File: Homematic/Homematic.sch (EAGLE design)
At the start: 28 parts, among them IC1 3.3V, IC2 3.3V, P1 DF11-06-2DS, Q1 BS170

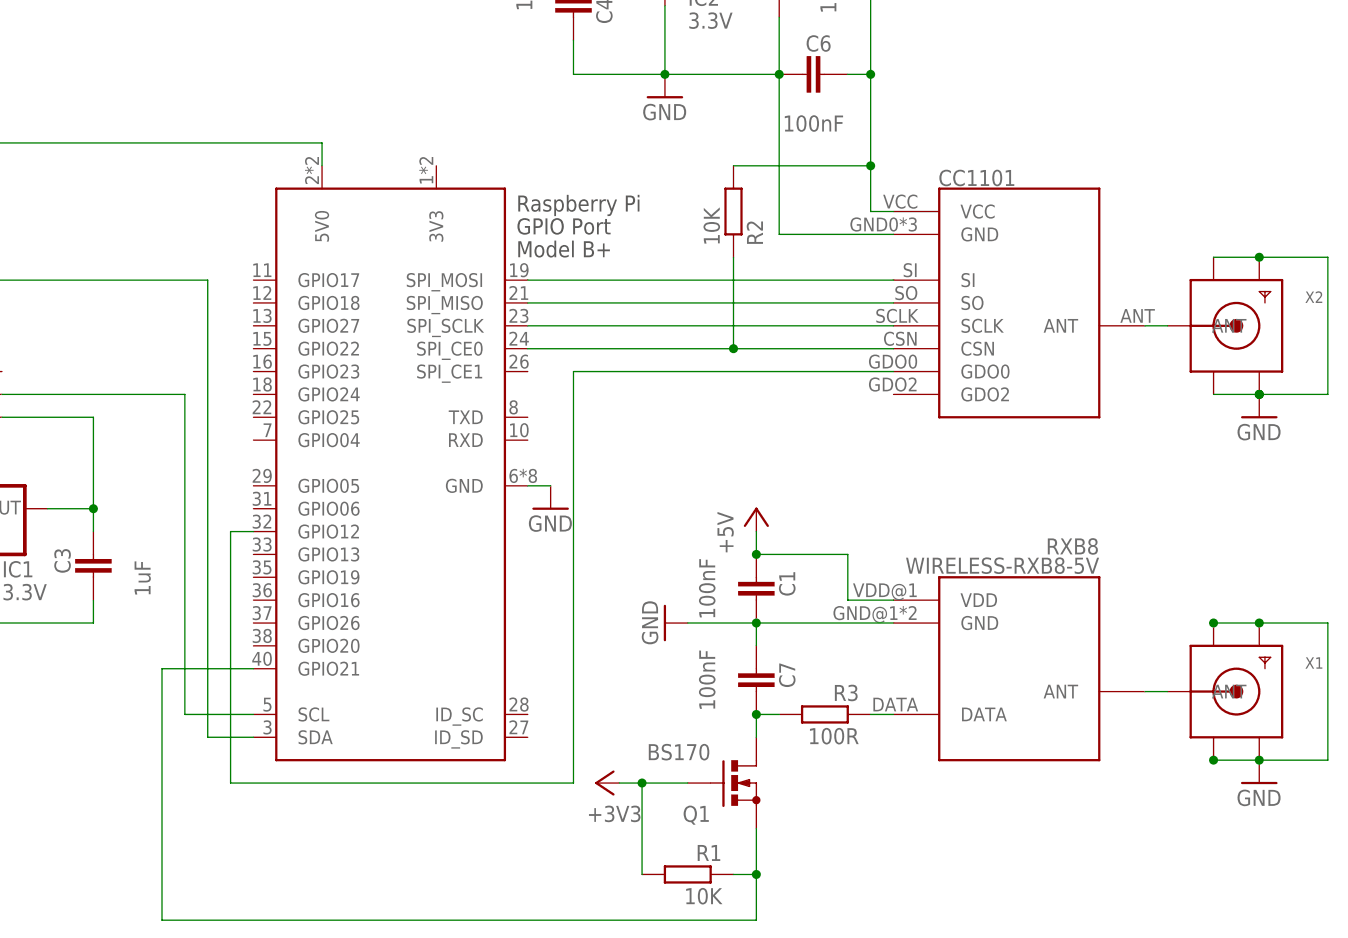
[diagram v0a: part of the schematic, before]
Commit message: Replace RXB8 with CC1101 receiver.
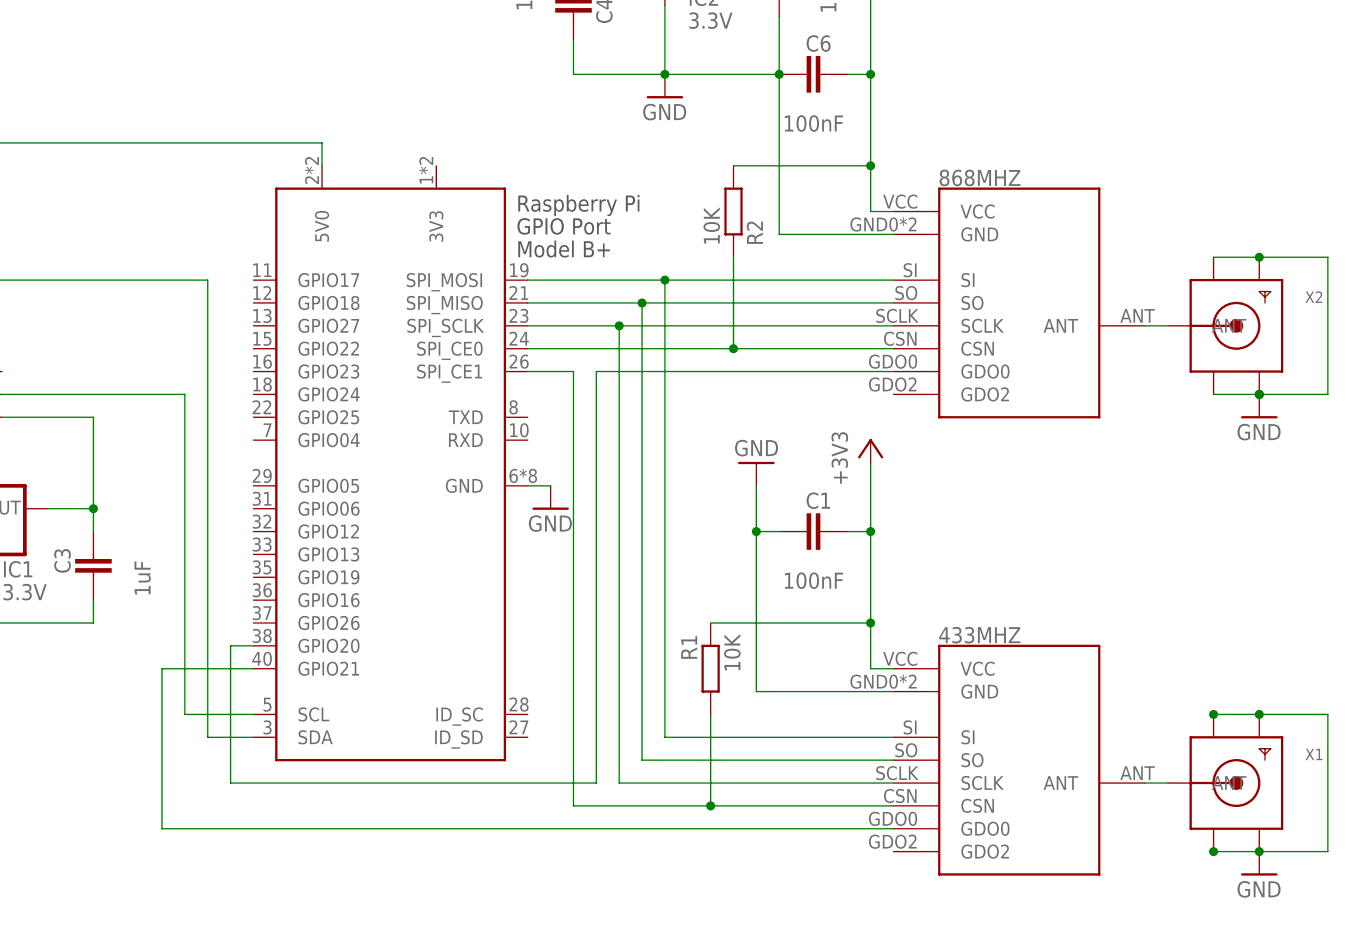
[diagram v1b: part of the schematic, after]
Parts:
- removed C7: 100nF, capacitor-wima:C2,5-3
- removed CC1101: CC1101SMD, modules:CC1101SMD
- removed Q1: BS170, transistor-small-signal:BS170
- removed R3: 100R, rcl:R-EU_0204/2V
- removed RXB8: WIRELESS-RXB8-5V, modules:WIRELESS-RXB8-5V
- added 433MHZ, 868MHZ: CC1101E07-SMD, modules:CC1101E07-SMD
- C2, C3, C4, C5: device capacitor-wima:C5/3 -> rcl:C-EUC0805
- R1: device rcl:R-EU_0204/2V -> rcl:R-EU_0204/5
- R2: device rcl:R-EU_0204/7 -> rcl:R-EU_0204/5
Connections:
- removed net N$11: C7.2, Q1.D, R3.2
- net +3V3: now also 433MHZ.VCC, 868MHZ.VCC, C1.1, R1.1; no longer CC1101.VCC, Q1.G, R1.2
- net +5V: no longer C1.1, RXB8.VDD
- net GND: now also 433MHZ.GND, 868MHZ.GND; no longer C7.1, CC1101.GND, RXB8.GND
- net N$10: now also 433MHZ.GDO0; no longer Q1.S, R1.1
- net N$15: now also 868MHZ.CSN; no longer CC1101.CSN
- net N$16: now also 433MHZ.SCLK, 868MHZ.SCLK; no longer CC1101.SCLK
- net N$17: now also 433MHZ.SO, 868MHZ.SO; no longer CC1101.SO
- net N$18: now also 433MHZ.SI, 868MHZ.SI; no longer CC1101.SI
- net N$19: now also 868MHZ.GDO0, RPI.GPIO20; no longer CC1101.GDO0, RPI.GPIO12
- net N$20: now also 868MHZ.ANT; no longer CC1101.ANT
- net N$3: now also 433MHZ.CSN, R1.2, RPI.SPI_CE1; no longer R3.1, RXB8.DATA
- net N$8: now also 433MHZ.ANT; no longer RXB8.ANT
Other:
- moved on the sheet: C1, R1, X1

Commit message: Fix export. Remove switch. Prepare board for production.
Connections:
- net N$15: now also RPI.SPI_CE1; no longer RPI.SPI_CE0
- net N$3: now also RPI.SPI_CE0; no longer RPI.SPI_CE1
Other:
- moved on the sheet: R1

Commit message: Fix footprint. Replace PTC.
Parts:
- F1: value 2A -> 3A; device SparkFun-Fuses:PPTCPTH -> SparkFun-Fuses:PPTCPTH11MM
- F2: value 2A -> 2.5A; device SparkFun-Fuses:PPTCPTH -> SparkFun-Fuses:PPTCPTH11MM
- F3: value 3A -> 2.5A
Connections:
- net +5V: now also F3.2; no longer F2.2
- net N$4: now also F2.2; no longer F1.2
- net N$5: now also F2.1; no longer F1.1
- net N$6: now also F3.1; no longer F2.1
- net N$7: now also F1.1; no longer F3.1
- net N$9: now also F1.2; no longer F3.2
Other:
- moved on the sheet: F1, F2, F3
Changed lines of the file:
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@@
 <part name="D1" library="diode" deviceset="1N5908" device=""/>
 <part name="D2" library="diode" deviceset="1N5908" device=""/>
-<part name="F1" library="SparkFun-Fuses" deviceset="PPTC" device="PTH" value="2A"/>
-<part name="F2" library="SparkFun-Fuses" deviceset="PPTC" device="PTH" value="2A"/>
+<part name="F2" library="SparkFun-Fuses" deviceset="PPTC" device="PTH11MM" value="2.5A"/>
+<part name="F3" library="SparkFun-Fuses" deviceset="PPTC" device="PTH11MM" value="2.5A"/>
 <part name="GND1" library="supply1" deviceset="GND" device=""/>
 <part name="P+1" library="supply1" deviceset="+24V" device=""/>
@@
 <part name="+3V2" library="supply1" deviceset="+3V3" device=""/>
 <part name="GND7" library="supply1" deviceset="GND" device=""/>
-<part name="F3" library="SparkFun-Fuses" deviceset="PPTC" device="PTH11MM" value="3A"/>
+<part name="F1" library="SparkFun-Fuses" deviceset="PPTC" device="PTH11MM" value="3A"/>
 <part name="433MHZ" library="modules" deviceset="CC1101" device="E07-SMD" value="CC1101E07-SMD"/>
 <part name="R1" library="rcl" deviceset="R-EU_" device="0204/5" value="10K">
@@
 <attribute name="VALUE" x="86.36" y="73.66" size="1.778" layer="96" rot="R270" align="top-center"/>
 </instance>
-<instance part="F1" gate="G$1" x="83.82" y="99.06" rot="R180"/>
-<instance part="F2" gate="G$1" x="81.28" y="58.42"/>
+<instance part="F2" gate="G$1" x="83.82" y="99.06" rot="R180"/>
+<instance part="F3" gate="G$1" x="81.28" y="58.42"/>
 <instance part="GND1" gate="1" x="68.58" y="78.74" rot="R270"/>
 <instance part="P+1" gate="1" x="15.24" y="91.44" smashed="yes">
@@
 <instance part="+3V2" gate="G$1" x="213.36" y="66.04"/>
 <instance part="GND7" gate="1" x="177.8" y="58.42"/>
-<instance part="F3" gate="G$1" x="35.56" y="81.28" rot="R180"/>
+<instance part="F1" gate="G$1" x="35.56" y="81.28" rot="R180"/>
 <instance part="433MHZ" gate="G$1" x="229.87" y="30.48"/>
 <instance part="R1" gate="G$1" x="198.12" y="40.64" rot="MR270">
@@
 <segment>
 <pinref part="MP1584-2" gate="G$1" pin="OUT+"/>
-<pinref part="F1" gate="G$1" pin="2"/>
+<pinref part="F2" gate="G$1" pin="2"/>
 <wire x1="73.66" y1="99.06" x2="76.2" y2="99.06" width="0.1524" layer="91"/>
 </segment>
@@
 <segment>
 <pinref part="MP1584-1" gate="G$1" pin="OUT+"/>
-<pinref part="F2" gate="G$1" pin="1"/>
+<pinref part="F3" gate="G$1" pin="1"/>
 <wire x1="73.66" y1="58.42" x2="76.2" y2="58.42" width="0.1524" layer="91"/>
 </segment>
@@
 <segment>
 <pinref part="D1" gate="1" pin="C"/>
-<pinref part="F1" gate="G$1" pin="1"/>
+<pinref part="F2" gate="G$1" pin="1"/>
 <wire x1="88.9" y1="99.06" x2="88.9" y2="86.36" width="0.1524" layer="91"/>
 <wire x1="88.9" y1="99.06" x2="152.4" y2="99.06" width="0.1524" layer="91"/>
@@
 </segment>
 <segment>
-<pinref part="F2" gate="G$1" pin="2"/>
+<pinref part="F3" gate="G$1" pin="2"/>
 <pinref part="D2" gate="1" pin="C"/>
 <wire x1="88.9" y1="68.58" x2="88.9" y2="71.12" width="0.1524" layer="91"/>
@@
 <wire x1="40.64" y1="81.28" x2="40.64" y2="58.42" width="0.1524" layer="91"/>
 <wire x1="40.64" y1="58.42" x2="43.18" y2="58.42" width="0.1524" layer="91"/>
-<pinref part="F3" gate="G$1" pin="1"/>
+<pinref part="F1" gate="G$1" pin="1"/>
 <junction x="40.64" y="81.28"/>
 </segment>
@@
 <segment>
 <pinref part="D3" gate="G$1" pin="C"/>
-<pinref part="F3" gate="G$1" pin="2"/>
-</segment>
-</net>
+<pinref part="F1" gate="G$1" pin="2"/>
+</segment>
+</net>

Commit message: Add fan circuit
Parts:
- added D4: 1N4148DO35-2V, diode:1N4148DO35-2V
- added FAN: 22-27-2021-02, con-molex:22-27-2021-02
- added Q1: BC337-40, transistor-npn:BC337-40
- added R3: 10K, rcl:R-EU_0204/2V
- added R4: 1K8, rcl:R-EU_0204/2V
- F1: device SparkFun-Fuses:PPTCPTH11MM -> ptc:PPTCPTH11MM
- F2, F3: value 2.5A -> 16V/2.5A; device SparkFun-Fuses:PPTCPTH11MM -> ptc:PPTCRGEF250
- R2: device rcl:R-EU_0204/5 -> rcl:R-EU_0204/2V
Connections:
- new net N$11: Q1.B, R3.2, R4.2
- new net N$13: R4.1, RPI.GPIO12
- new net N$14: D4.A, FAN-2.S, Q1.C
- net +5V: now also D4.C, FAN-1.S
- net GND: now also Q1.E, R3.1
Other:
- note added: "+Fan"
- note added: "-Fan"

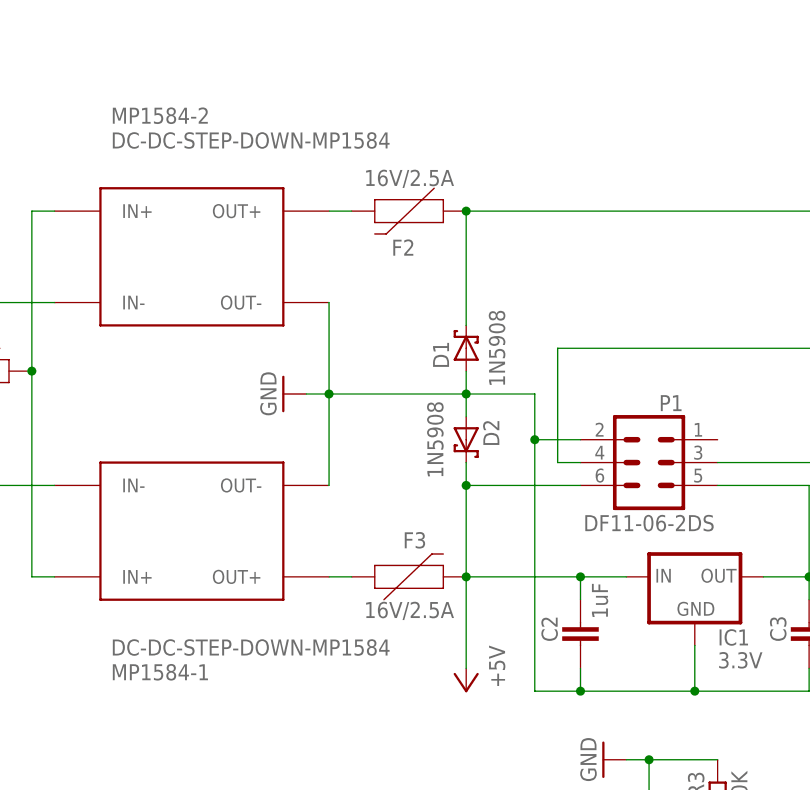
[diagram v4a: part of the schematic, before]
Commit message: Use SMD PTC's instead of through hole ones.
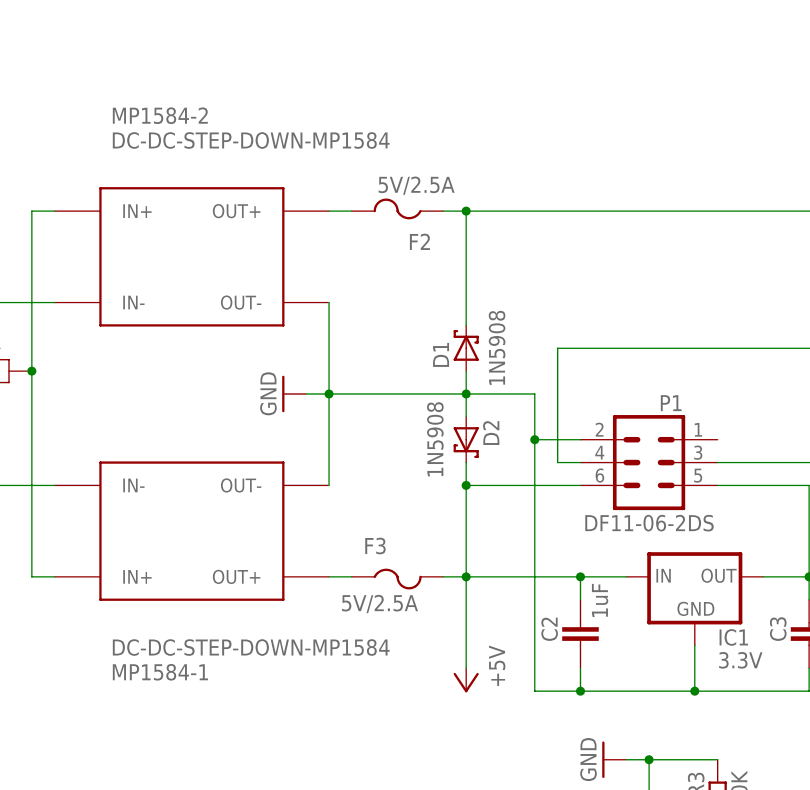
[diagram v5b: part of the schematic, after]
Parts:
- F2, F3: value 16V/2.5A -> 5V/2.5A; device ptc:PPTCRGEF250 -> adafruit:PTCFUSE-1812
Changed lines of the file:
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@@
 <part name="D1" library="diode" deviceset="1N5908" device=""/>
 <part name="D2" library="diode" deviceset="1N5908" device=""/>
-<part name="F2" library="ptc" deviceset="PPTC" device="RGEF250" value="16V/2.5A"/>
-<part name="F3" library="ptc" deviceset="PPTC" device="RGEF250" value="16V/2.5A"/>
+<part name="F2" library="adafruit" deviceset="PTCFUSE" device="-1812" value="5V/2.5A"/>
+<part name="F3" library="adafruit" deviceset="PTCFUSE" device="-1812" value="5V/2.5A"/>
 <part name="GND1" library="supply1" deviceset="GND" device=""/>
 <part name="P+1" library="supply1" deviceset="+24V" device=""/>
@@
 <attribute name="VALUE" x="86.36" y="73.66" size="1.778" layer="96" rot="R270" align="top-center"/>
 </instance>
-<instance part="F2" gate="G$1" x="83.82" y="99.06" rot="R180"/>
-<instance part="F3" gate="G$1" x="81.28" y="58.42"/>
+<instance part="F2" gate="G$1" x="81.28" y="101.6" smashed="yes" rot="R180">
+<attribute name="VALUE" x="87.63" y="102.87" size="1.778" layer="96" rot="R180"/>
+<attribute name="NAME" x="85.09" y="96.52" size="1.778" layer="95" rot="R180"/>
+</instance>
+<instance part="F3" gate="G$1" x="81.28" y="55.88" smashed="yes">
+<attribute name="VALUE" x="74.93" y="54.61" size="1.778" layer="96"/>
+<attribute name="NAME" x="77.47" y="60.96" size="1.778" layer="95"/>
+</instance>
 <instance part="GND1" gate="1" x="68.58" y="78.74" rot="R270"/>
 <instance part="P+1" gate="1" x="15.24" y="91.44" smashed="yes">
@@
 <pinref part="F2" gate="G$1" pin="1"/>
 <wire x1="88.9" y1="99.06" x2="88.9" y2="86.36" width="0.1524" layer="91"/>
+<wire x1="86.36" y1="99.06" x2="88.9" y2="99.06" width="0.1524" layer="91"/>
+<pinref part="RPI" gate="G$1" pin="5V0"/>
 <wire x1="88.9" y1="99.06" x2="152.4" y2="99.06" width="0.1524" layer="91"/>
+<wire x1="152.4" y1="99.06" x2="152.4" y2="96.52" width="0.1524" layer="91"/>
 <junction x="88.9" y="99.06"/>
-<pinref part="RPI" gate="G$1" pin="5V0"/>
-<wire x1="152.4" y1="99.06" x2="152.4" y2="96.52" width="0.1524" layer="91"/>
 </segment>
 </net>
@@
 <junction x="88.9" y="68.58"/>
 <wire x1="88.9" y1="68.58" x2="88.9" y2="58.42" width="0.1524" layer="91"/>
-<junction x="88.9" y="58.42"/>
 <pinref part="IC1" gate="1" pin="IN"/>
+<pinref part="C2" gate="G$1" pin="1"/>
 <wire x1="88.9" y1="58.42" x2="101.6" y2="58.42" width="0.1524" layer="91"/>
-<pinref part="C2" gate="G$1" pin="1"/>
 <wire x1="101.6" y1="55.88" x2="101.6" y2="58.42" width="0.1524" layer="91"/>
 <wire x1="101.6" y1="58.42" x2="106.68" y2="58.42" width="0.1524" layer="91"/>
 <junction x="101.6" y="58.42"/>
 <pinref part="P+3" gate="1" pin="+5V"/>
+<wire x1="86.36" y1="58.42" x2="88.9" y2="58.42" width="0.1524" layer="91"/>
 <wire x1="88.9" y1="58.42" x2="88.9" y2="48.26" width="0.1524" layer="91"/>
-</segment>
-<segment>
+<junction x="88.9" y="58.42"/>
+</segment>
+<segment>
